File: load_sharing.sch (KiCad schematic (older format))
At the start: 2 parts, among them Q2 NTLJF3117P

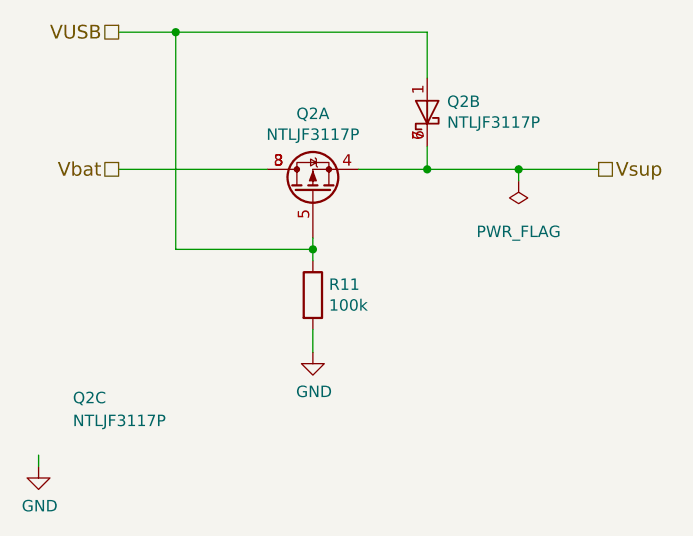
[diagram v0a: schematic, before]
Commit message: Fixed NTLJF3117P MOSFET pin layout
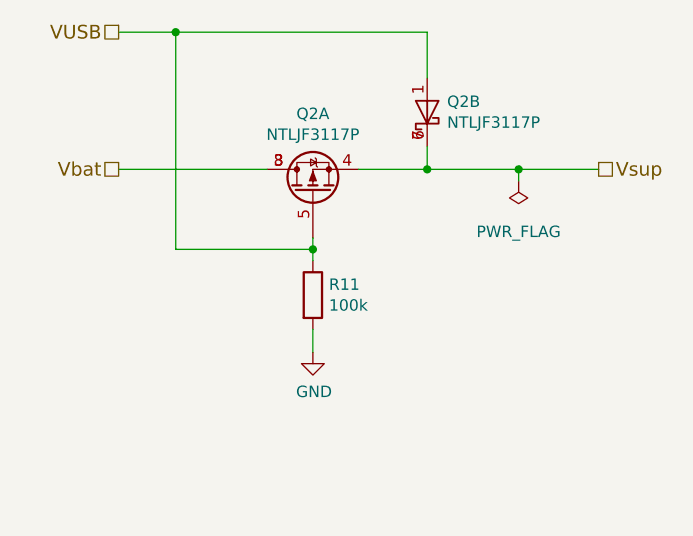
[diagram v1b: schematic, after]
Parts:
- removed unit 3 of Q2
- Q2: footprint TO_SOT_Packages_THT:TO-92_Molded_Narrow -> Custom_footprints:DFN-6-2EP_2x2mm_Pitch0.65mm; MFN (none) -> On Semiconductor; MFP (none) -> NTLJF3117PT1G
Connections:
- wire segments 11 -> 10
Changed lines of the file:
@@
 F 0 "Q2" V 4843 3200 50  0000 C CNN
 F 1 "NTLJF3117P" V 4752 3200 50  0000 C CNN
-F 2 "TO_SOT_Packages_THT:TO-92_Molded_Narrow" H 4700 3125 50  0001 L CIN
+F 2 "Custom_footprints:DFN-6-2EP_2x2mm_Pitch0.65mm" H 4700 3125 50  0001 L CIN
 F 3 "" H 4500 3200 50  0001 L CNN
+F 4 "On Semiconductor" H 4500 3200 60  0001 C CNN "MFN"
+F 5 "NTLJF3117PT1G" H 4500 3200 60  0001 C CNN "MFP"
 	1    4500 3200
 	0    -1   -1   0
@@
 F 0 "Q2" V 5046 2763 50  0000 R CNN
 F 1 "NTLJF3117P" V 4955 2763 50  0000 R CNN
-F 2 "TO_SOT_Packages_THT:TO-92_Molded_Narrow" H 5200 2775 50  0001 L CIN
+F 2 "Custom_footprints:DFN-6-2EP_2x2mm_Pitch0.65mm" H 5200 2775 50  0001 L CIN
 F 3 "" H 5000 2850 50  0001 L CNN
+F 4 "On Semiconductor" H 5000 2850 60  0001 C CNN "MFN"
+F 5 "NTLJF3117PT1G" H 5000 2850 60  0001 C CNN "MFP"
 	2    5000 2850
 	0    -1   -1   0
 $EndComp
-$Comp
-L NTLJF3117P Q2
-U 3 1 59D1228C
-P 3200 4150
-F 0 "Q2" H 3450 4200 50  0000 L CNN
-F 1 "NTLJF3117P" H 3450 4100 50  0000 L CNN
-F 2 "Custom_footprints:DFN-6-2EP_2x2mm_Pitch0.65mm" H 3400 4075 50  0001 L CIN
-F 3 "" H 3400 4225 50  0001 L CNN
-F 4 "NTLJF3117PT1G" H 3600 4425 60  0001 C CNN "MFP"
-F 5 "On Semiconductor" H 3500 4325 60  0001 C CNN "MFN"
-	3    3200 4150
-	1    0    0    -1
-$EndComp
-$Comp
-L GND #PWR011
-U 1 1 59D1233A
-P 3300 4400
-F 0 "#PWR011" H 3300 4150 50  0001 C CNN
-F 1 "GND" H 3305 4227 50  0000 C CNN
-F 2 "" H 3300 4400 50  0000 C CNN
-F 3 "" H 3300 4400 50  0000 C CNN
-	1    3300 4400
-	1    0    0    -1
-$EndComp
-Wire Wire Line
-	3300 4350 3300 4400
 $EndSCHEMATC

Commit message: Moved MCU pins around to make sure that they do not interfere with the programmer Moved ISP Header closer to the edge of the board to allow easier access with the programmer Added pulldown resistor to the DCD/DC converters enable pin to make sure it stays off in case of failure Added more PDFs of components
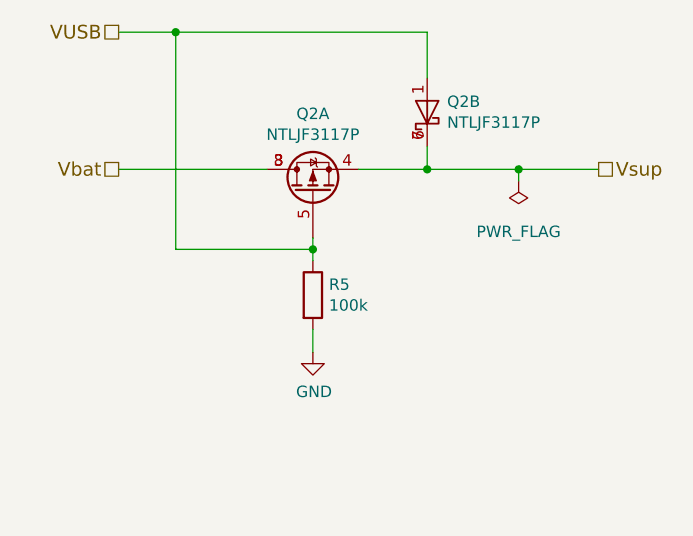
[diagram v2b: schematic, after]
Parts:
- renumbered R11 to R5
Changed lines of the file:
@@
 	4300 3100 3650 3100
 $Comp
-L R R11
+L R R5
 U 1 1 58AA6169
 P 4500 3650
-F 0 "R11" H 4570 3696 50  0000 L CNN
+F 0 "R5" H 4570 3696 50  0000 L CNN
 F 1 "100k" H 4570 3605 50  0000 L CNN
 F 2 "Resistors_SMD:R_0603" H 4570 3559 50  0001 L CNN

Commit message: Added part names and BOM Added Gerber files
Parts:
- R5: MFN (none) -> Yageo; MFP (none) -> RC0603JR-07100KL
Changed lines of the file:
@@
 F 2 "Resistors_SMD:R_0603" H 4570 3559 50  0001 L CNN
 F 3 "" H 4500 3650 50  0000 C CNN
+F 4 "Yageo" H 4500 3650 60  0001 C CNN "MFN"
+F 5 "RC0603JR-07100KL" H 4500 3650 60  0001 C CNN "MFP"
 	1    4500 3650
 	1    0    0    -1

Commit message: Preparing for v1.2 Updated to KiCAD 5 nightly Added resistors to isolate the programming pins Added transistor to drive the LED Replaced LTC3458 boost converter with an LTC3536 buck-boost converter to step down the USB power supply Added debugging jumper to test the voltage regulator
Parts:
- Q2: symbol NTLJF3117P -> On-Semiconductor:NTLJF3117P
- R5: symbol R -> device:R
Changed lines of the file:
@@
-EESchema Schematic File Version 2
-LIBS:power
-LIBS:device
-LIBS:transistors
-LIBS:conn
-LIBS:linear
-LIBS:regul
-LIBS:74xx
-LIBS:cmos4000
-LIBS:adc-dac
-LIBS:memory
-LIBS:xilinx
-LIBS:microcontrollers
-LIBS:dsp
-LIBS:microchip
-LIBS:analog_switches
-LIBS:motorola
-LIBS:texas
-LIBS:intel
-LIBS:audio
-LIBS:interface
-LIBS:digital-audio
-LIBS:philips
-LIBS:display
-LIBS:cypress
-LIBS:siliconi
-LIBS:opto
-LIBS:atmel
-LIBS:contrib
-LIBS:valves
-LIBS:switches
-LIBS:Microchip
-LIBS:On Semiconductor
-LIBS:Linear Technology
+EESchema Schematic File Version 4
 LIBS:main-cache
 EELAYER 26 0
@@
 	4300 3100 3650 3100
 $Comp
-L R R5
+L device:R R5
 U 1 1 58AA6169
 P 4500 3650
@@
 $EndComp
 $Comp
-L GND #PWR09
+L power:GND #PWR09
 U 1 1 58AA61A7
 P 4500 3900
@@
 $EndComp
 Wire Wire Line
-	4500 3400 4500 3500
+	4500 3400 4500 3450
 Wire Wire Line
 	4500 3800 4500 3900
@@
 	5000 3000 5000 3100
 Wire Wire Line
-	4700 3100 5750 3100
+	4700 3100 5000 3100
 Connection ~ 5000 3100
 Wire Wire Line
-	3650 2500 5000 2500
+	3650 2500 3900 2500
 Wire Wire Line
 	5000 2500 5000 2700
@@
 Connection ~ 3900 2500
 $Comp
-L PWR_FLAG #FLG010
+L power:PWR_FLAG #FLG01
 U 1 1 58AAB840
 P 5400 3150
-F 0 "#FLG010" H 5400 3245 50  0001 C CNN
+F 0 "#FLG01" H 5400 3245 50  0001 C CNN
 F 1 "PWR_FLAG" H 5400 3373 50  0000 C CNN
 F 2 "" H 5400 3150 50  0000 C CNN
@@
 Connection ~ 5400 3100
 $Comp
-L NTLJF3117P Q2
+L On-Semiconductor:NTLJF3117P Q2
 U 1 1 59D0546A
 P 4500 3200
@@
 $EndComp
 $Comp
-L NTLJF3117P Q2
+L On-Semiconductor:NTLJF3117P Q2
 U 2 1 59D055B2
 P 5000 2850
@@
 	0    -1   -1   0
 $EndComp
+Wire Wire Line
+	5000 3100 5400 3100
+Wire Wire Line
+	4500 3450 4500 3500
+Wire Wire Line
+	3900 2500 5000 2500
+Wire Wire Line
+	5400 3100 5750 3100
 $EndSCHEMATC

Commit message: Updated to Kicad v5.0
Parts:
- R5: symbol device:R -> Device:R
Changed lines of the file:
@@
 	4300 3100 3650 3100
 $Comp
-L device:R R5
+L Device:R R5
 U 1 1 58AA6169
 P 4500 3650

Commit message: Added power on state LED Updated to KiCAD 5.0
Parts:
- R5: footprint Resistors_SMD:R_0603 -> Resistor_SMD:R_0603_1608Metric
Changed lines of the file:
@@
 F 0 "R5" H 4570 3696 50  0000 L CNN
 F 1 "100k" H 4570 3605 50  0000 L CNN
-F 2 "Resistors_SMD:R_0603" H 4570 3559 50  0001 L CNN
+F 2 "Resistor_SMD:R_0603_1608Metric" H 4570 3559 50  0001 L CNN
 F 3 "" H 4500 3650 50  0000 C CNN
 F 4 "Yageo" H 4500 3650 60  0001 C CNN "MFN"
